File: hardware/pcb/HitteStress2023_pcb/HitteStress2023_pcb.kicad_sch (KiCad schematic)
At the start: 0 parts

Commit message: Started drawing
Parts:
- added P1: ~, symbol my-KiCad-library:HLK-5M05
- added S1: ~, symbol my-KiCad-library:AM2315C
- added S2: ~, symbol my-KiCad-library:SPS30
- added U1: ~, symbol my-KiCad-library:TTGO_T-Beam_T22_V1.1
- added U2: ~, symbol my-KiCad-library:MINIDCDCBOOST5V
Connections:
- new net GND: S1.4 (GND), S2.5 (GND), U1.12 (GND), U1.19 (GND), U1.21 (GND)
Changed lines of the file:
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@@
 (kicad_sch (version 20230121) (generator eeschema)
   (paper "A4")
+  (wire (pts (xy 105.41 77.47) (xy 120.65 77.47))
+    (stroke (width 0) (type default))
+  )
+  (wire (pts (xy 151.13 92.71) (xy 166.37 92.71))
+    (stroke (width 0) (type default))
+  )
+  (wire (pts (xy 193.04 105.41) (xy 177.8 105.41))
+    (stroke (width 0) (type default))
+  )
+  (wire (pts (xy 177.8 72.39) (xy 193.04 72.39))
+    (stroke (width 0) (type default))
+  )
+  (wire (pts (xy 105.41 82.55) (xy 120.65 82.55))
+    (stroke (width 0) (type default))
+  )
+  (label "GND" (at 179.07 72.39 0) (fields_autoplaced)
+    (effects (font (size 1.27 1.27)) (justify left bottom))
+  )
+  (label "GND" (at 106.68 82.55 0) (fields_autoplaced)
+    (effects (font (size 1.27 1.27)) (justify left bottom))
+  )
+  (label "GND" (at 165.1 92.71 180) (fields_autoplaced)
+    (effects (font (size 1.27 1.27)) (justify right bottom))
+  )
+  (label "GND" (at 179.07 105.41 0) (fields_autoplaced)
+    (effects (font (size 1.27 1.27)) (justify left bottom))
+  )
+  (label "GND" (at 106.68 77.47 0) (fields_autoplaced)
+    (effects (font (size 1.27 1.27)) (justify left bottom))
+  )
+  (symbol (lib_id "my-KiCad-library:TTGO_T-Beam_T22_V1.1") (at 135.89 80.01 0) (unit 1)
+    (in_bom yes) (on_board yes) (dnp no) (fields_autoplaced)
+    (property "Reference" "U1" (at 135.89 55.88 0)
+      (effects (font (size 1.27 1.27)))
+    )
+    (property "Value" "~" (at 135.89 80.01 0)
+      (effects (font (size 1.27 1.27)))
+    )
+    (property "Footprint" "" (at 135.89 80.01 0)
+      (effects (font (size 1.27 1.27)) hide)
+    )
+    (property "Datasheet" "" (at 135.89 80.01 0)
+      (effects (font (size 1.27 1.27)) hide)
+    )
+    (pin "4")
+    (pin "25")
+    (pin "11")
+    (pin "3")
+    (pin "15")
+    (pin "6")
+    (pin "8")
+    (pin "7")
+    (pin "17")
+    (pin "2")
+    (pin "1")
+    (pin "24")
+    (pin "23")
+    (pin "5")
+    (pin "9")
+    (pin "13")
+    (pin "16")
+    (pin "22")
+    (pin "21")
+    (pin "14")
+    (pin "19")
+    (pin "26")
+    (pin "18")
+    (pin "12")
+    (pin "20")
+    (pin "10")
+    (instances
+      (project "HitteStress2023_pcb"
+        (path "/0b1ba7fb-a496-4717-8ed8-2a7de64e001c"
+          (reference "U1") (unit 1)
+        )
+      )
+    )
+  )
+  (symbol (lib_id "my-KiCad-library:MINIDCDCBOOST5V") (at 78.74 96.52 0) (unit 1)
+    (in_bom yes) (on_board yes) (dnp no) (fields_autoplaced)
+    (property "Reference" "U2" (at 81.26 85.09 0)
+      (effects (font (size 1.27 1.27)))
+    )
+    (property "Value" "~" (at 78.74 96.52 0)
+      (effects (font (size 1.27 1.27)))
+    )
+    (property "Footprint" "" (at 78.74 96.52 0)
+      (effects (font (size 1.27 1.27)) hide)
+    )
+    (property "Datasheet" "https://www.tinytronics.nl/shop/nl/power/spanningsconverters/boost-(step-up)-converters/mini-dc-dc-5v-step-up-boost-converter-480ma" (at 78.74 119.38 0)
+      (effects (font (size 1.27 1.27)) hide)
+    )
+    (pin "2")
+    (pin "3")
+    (pin "1")
+    (instances
+      (project "HitteStress2023_pcb"
+        (path "/0b1ba7fb-a496-4717-8ed8-2a7de64e001c"
+          (reference "U2") (unit 1)
+        )
+      )
+    )
+  )
+  (symbol (lib_id "my-KiCad-library:AM2315C") (at 203.2 68.58 0) (unit 1)
+    (in_bom yes) (on_board yes) (dnp no) (fields_autoplaced)
+    (property "Reference" "S1" (at 210.82 67.4342 0)
+      (effects (font (size 1.27 1.27)) (justify left))
+    )
+    (property "Value" "~" (at 199.39 68.58 0)
+      (effects (font (size 1.27 1.27)))
+    )
+    (property "Footprint" "" (at 199.39 68.58 0)
+      (effects (font (size 1.27 1.27)) hide)
+    )
+    (property "Datasheet" "https://cdn-shop.adafruit.com/product-files/5182/5182_AM2315C.pdf" (at 199.39 81.28 0)
+      (effects (font (size 1.27 1.27)) hide)
+    )
+    (pin "1")
+    (pin "4")
+    (pin "3")
+    (pin "2")
+    (instances
+      (project "HitteStress2023_pcb"
+        (path "/0b1ba7fb-a496-4717-8ed8-2a7de64e001c"
+          (reference "S1") (unit 1)
+        )
+      )
+    )
+  )
+  (symbol (lib_id "my-KiCad-library:SPS30") (at 203.2 100.33 0) (unit 1)
+    (in_bom yes) (on_board yes) (dnp no) (fields_autoplaced)
+    (property "Reference" "S2" (at 212.09 99.1842 0)
+      (effects (font (size 1.27 1.27)) (justify left))
+    )
+    (property "Value" "~" (at 203.2 100.33 0)
+      (effects (font (size 1.27 1.27)))
+    )
+    (property "Footprint" "" (at 203.2 100.33 0)
+      (effects (font (size 1.27 1.27)) hide)
+    )
+    (property "Datasheet" "https://sensirion.com/media/documents/8600FF88/616542B5/Sensirion_PM_Sensors_Datasheet_SPS30.pdf" (at 203.2 113.03 0)
+      (effects (font (size 1.27 1.27)) hide)
+    )
+    (pin "5")
+    (pin "4")
+    (pin "1")
+    (pin "2")
+    (pin "3")
+    (instances
+      (project "HitteStress2023_pcb"
+        (path "/0b1ba7fb-a496-4717-8ed8-2a7de64e001c"
+          (reference "S2") (unit 1)
+        )
+      )
+    )
+  )
+  (symbol (lib_id "my-KiCad-library:HLK-5M05") (at 63.5 63.5 0) (unit 1)
+    (in_bom yes) (on_board yes) (dnp no) (fields_autoplaced)
+    (property "Reference" "P1" (at 63.4142 53.34 0)
+      (effects (font (size 1.27 1.27)))
+    )
+    (property "Value" "~" (at 63.5 63.5 0)
+      (effects (font (size 1.27 1.27)))
+    )
+    (property "Footprint" "" (at 63.5 63.5 0)
+      (effects (font (size 1.27 1.27)) hide)
+    )
+    (property "Datasheet" "https://5.imimg.com/data5/JI/JR/RP/SELLER-1833510/hlk-5m05-power-module.pdf" (at 63.5 72.39 0)
+      (effects (font (size 1.27 1.27)) hide)
+    )
+    (pin "1")
+    (pin "4")
+    (pin "3")
+    (pin "2")
+    (instances
+      (project "HitteStress2023_pcb"
+        (path "/0b1ba7fb-a496-4717-8ed8-2a7de64e001c"
+          (reference "P1") (unit 1)
+        )
+      )
+    )
+  )
   (sheet_instances
     (path "/" (page "1"))

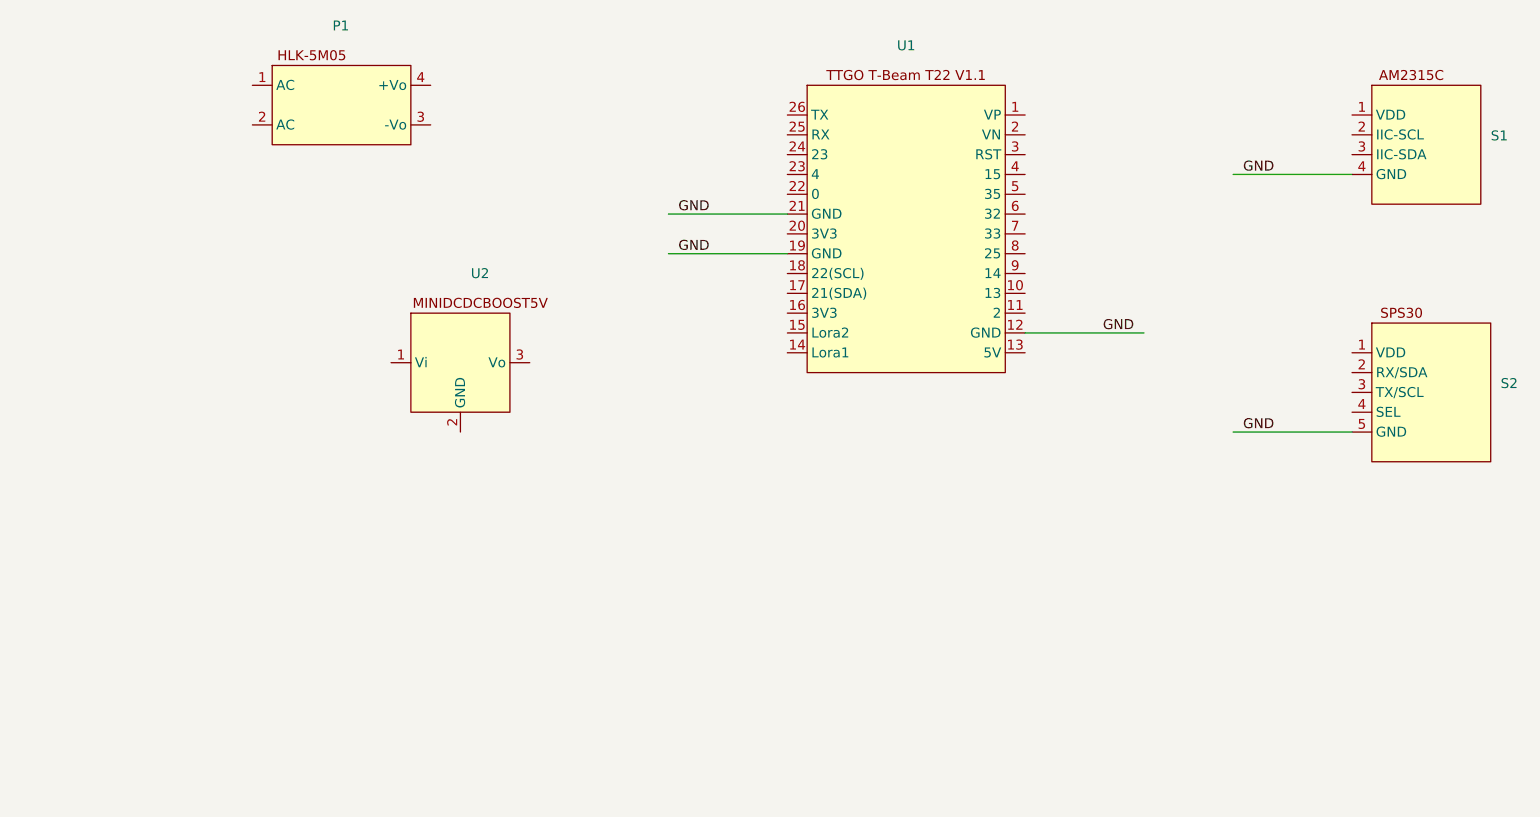
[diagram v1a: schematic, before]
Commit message: Drawing progress, added mandatory component to BOM Hittestress Homerus 2023.xlsx
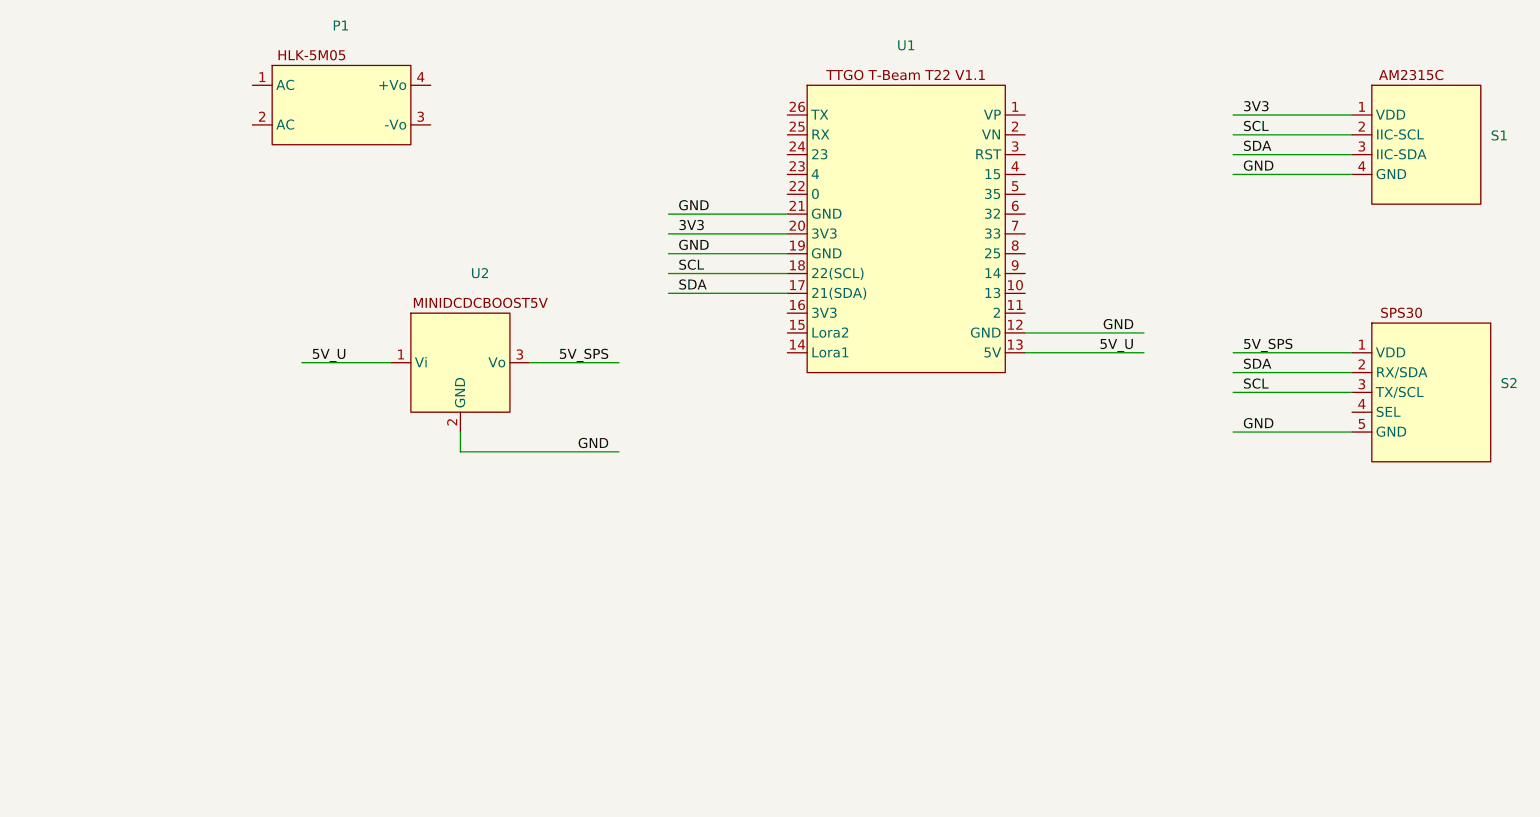
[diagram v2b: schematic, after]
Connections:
- net GND: now also U2.2 (GND)
- net 5V_U: now reaches U1.13 (5V)
- net 5V_U: now also U2.1 (Vi)
- net SDA: now reaches U1.17 (21(SDA))
- net SDA: now also S1.3 (IIC-SDA), S2.2 (RX/SDA)
- net SCL: now reaches U1.18 (22(SCL))
- net SCL: now also S1.2 (IIC-SCL), S2.3 (TX/SCL)
- net 3V3: now reaches U1.20 (3V3)
- net 3V3: now also S1.1 (VDD)
- net 5V_SPS: now reaches U2.3 (Vo)
- net 5V_SPS: now also S2.1 (VDD)
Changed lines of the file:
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@@
 (kicad_sch (version 20230121) (generator eeschema)
   (paper "A4")
+  (wire (pts (xy 177.8 64.77) (xy 193.04 64.77))
+    (stroke (width 0) (type default))
+  )
+  (wire (pts (xy 177.8 97.79) (xy 193.04 97.79))
+    (stroke (width 0) (type default))
+  )
   (wire (pts (xy 105.41 77.47) (xy 120.65 77.47))
+    (stroke (width 0) (type default))
+  )
+  (wire (pts (xy 105.41 87.63) (xy 120.65 87.63))
+    (stroke (width 0) (type default))
+  )
+  (wire (pts (xy 78.74 107.95) (xy 99.06 107.95))
     (stroke (width 0) (type default))
   )
@@
     (stroke (width 0) (type default))
   )
+  (wire (pts (xy 105.41 80.01) (xy 120.65 80.01))
+    (stroke (width 0) (type default))
+  )
+  (wire (pts (xy 87.63 96.52) (xy 99.06 96.52))
+    (stroke (width 0) (type default))
+  )
   (wire (pts (xy 177.8 72.39) (xy 193.04 72.39))
+    (stroke (width 0) (type default))
+  )
+  (wire (pts (xy 151.13 95.25) (xy 166.37 95.25))
+    (stroke (width 0) (type default))
+  )
+  (wire (pts (xy 58.42 96.52) (xy 69.85 96.52))
     (stroke (width 0) (type default))
   )
@@
     (stroke (width 0) (type default))
   )
+  (wire (pts (xy 177.8 69.85) (xy 193.04 69.85))
+    (stroke (width 0) (type default))
+  )
+  (wire (pts (xy 105.41 85.09) (xy 120.65 85.09))
+    (stroke (width 0) (type default))
+  )
+  (wire (pts (xy 78.74 105.41) (xy 78.74 107.95))
+    (stroke (width 0) (type default))
+  )
+  (wire (pts (xy 177.8 67.31) (xy 193.04 67.31))
+    (stroke (width 0) (type default))
+  )
+  (wire (pts (xy 177.8 100.33) (xy 193.04 100.33))
+    (stroke (width 0) (type default))
+  )
+  (wire (pts (xy 177.8 95.25) (xy 193.04 95.25))
+    (stroke (width 0) (type default))
+  )
+  (label "5V_U" (at 165.1 95.25 180) (fields_autoplaced)
+    (effects (font (size 1.27 1.27)) (justify right bottom))
+  )
   (label "GND" (at 179.07 72.39 0) (fields_autoplaced)
     (effects (font (size 1.27 1.27)) (justify left bottom))
   )
+  (label "SCL" (at 106.68 85.09 0) (fields_autoplaced)
+    (effects (font (size 1.27 1.27)) (justify left bottom))
+  )
+  (label "GND" (at 97.79 107.95 180) (fields_autoplaced)
+    (effects (font (size 1.27 1.27)) (justify right bottom))
+  )
   (label "GND" (at 106.68 82.55 0) (fields_autoplaced)
+    (effects (font (size 1.27 1.27)) (justify left bottom))
+  )
+  (label "5V_U" (at 59.69 96.52 0) (fields_autoplaced)
+    (effects (font (size 1.27 1.27)) (justify left bottom))
+  )
+  (label "3V3" (at 106.68 80.01 0) (fields_autoplaced)
+    (effects (font (size 1.27 1.27)) (justify left bottom))
+  )
+  (label "3V3" (at 179.07 64.77 0) (fields_autoplaced)
     (effects (font (size 1.27 1.27)) (justify left bottom))
   )
@@
     (effects (font (size 1.27 1.27)) (justify right bottom))
   )
+  (label "5V_SPS" (at 179.07 95.25 0) (fields_autoplaced)
+    (effects (font (size 1.27 1.27)) (justify left bottom))
+  )
+  (label "SCL" (at 179.07 67.31 0) (fields_autoplaced)
+    (effects (font (size 1.27 1.27)) (justify left bottom))
+  )
+  (label "5V_SPS" (at 97.79 96.52 180) (fields_autoplaced)
+    (effects (font (size 1.27 1.27)) (justify right bottom))
+  )
+  (label "SDA" (at 106.68 87.63 0) (fields_autoplaced)
+    (effects (font (size 1.27 1.27)) (justify left bottom))
+  )
   (label "GND" (at 179.07 105.41 0) (fields_autoplaced)
     (effects (font (size 1.27 1.27)) (justify left bottom))
   )
+  (label "SDA" (at 179.07 69.85 0) (fields_autoplaced)
+    (effects (font (size 1.27 1.27)) (justify left bottom))
+  )
+  (label "SDA" (at 179.07 97.79 0) (fields_autoplaced)
+    (effects (font (size 1.27 1.27)) (justify left bottom))
+  )
+  (label "SCL" (at 179.07 100.33 0) (fields_autoplaced)
+    (effects (font (size 1.27 1.27)) (justify left bottom))
+  )
